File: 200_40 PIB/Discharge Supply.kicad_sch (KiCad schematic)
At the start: 57 parts, among them Q1 EPC2302, T1 Arthur, U1 LM5022MM, U2 TLVH431BQDCKT, U3 LTV-817-C

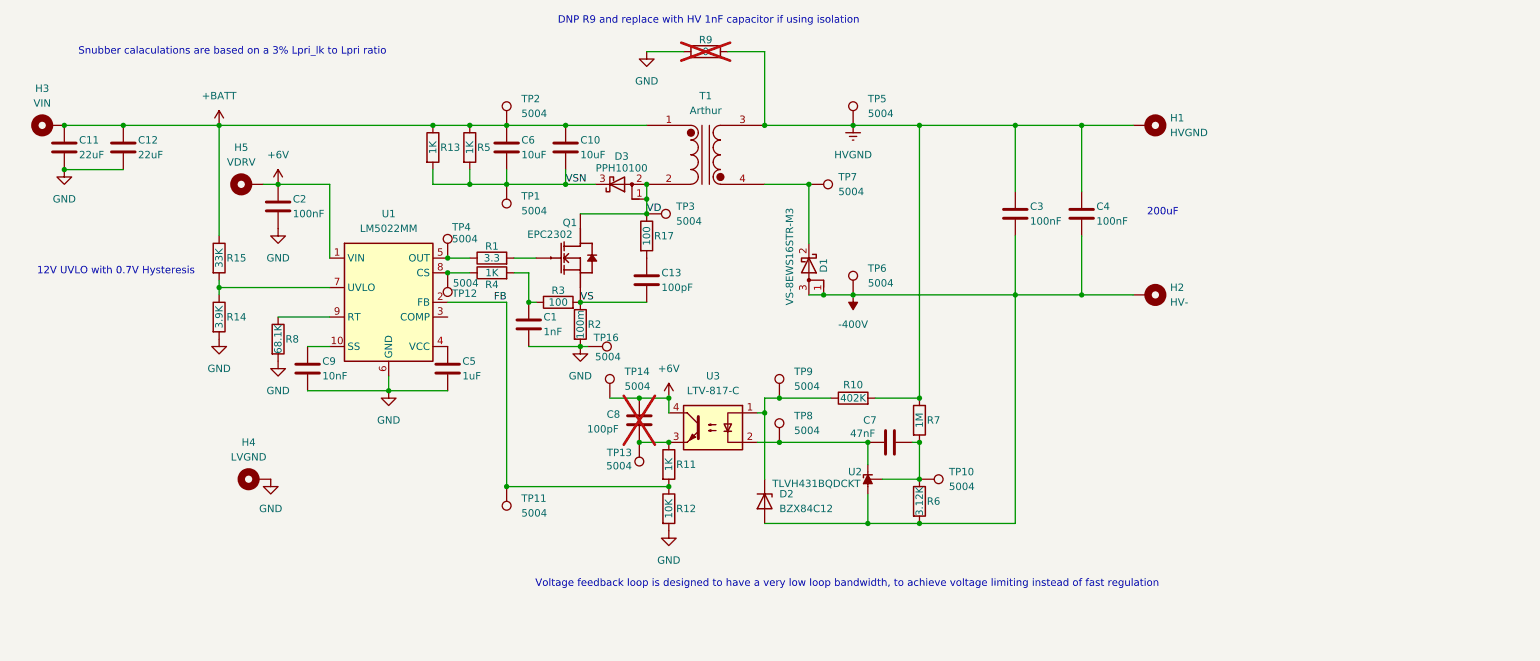
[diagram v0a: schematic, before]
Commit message: Summer 2026 Updates
Created symbol, footprint, and 3D model libraries. Redesigned PIB.
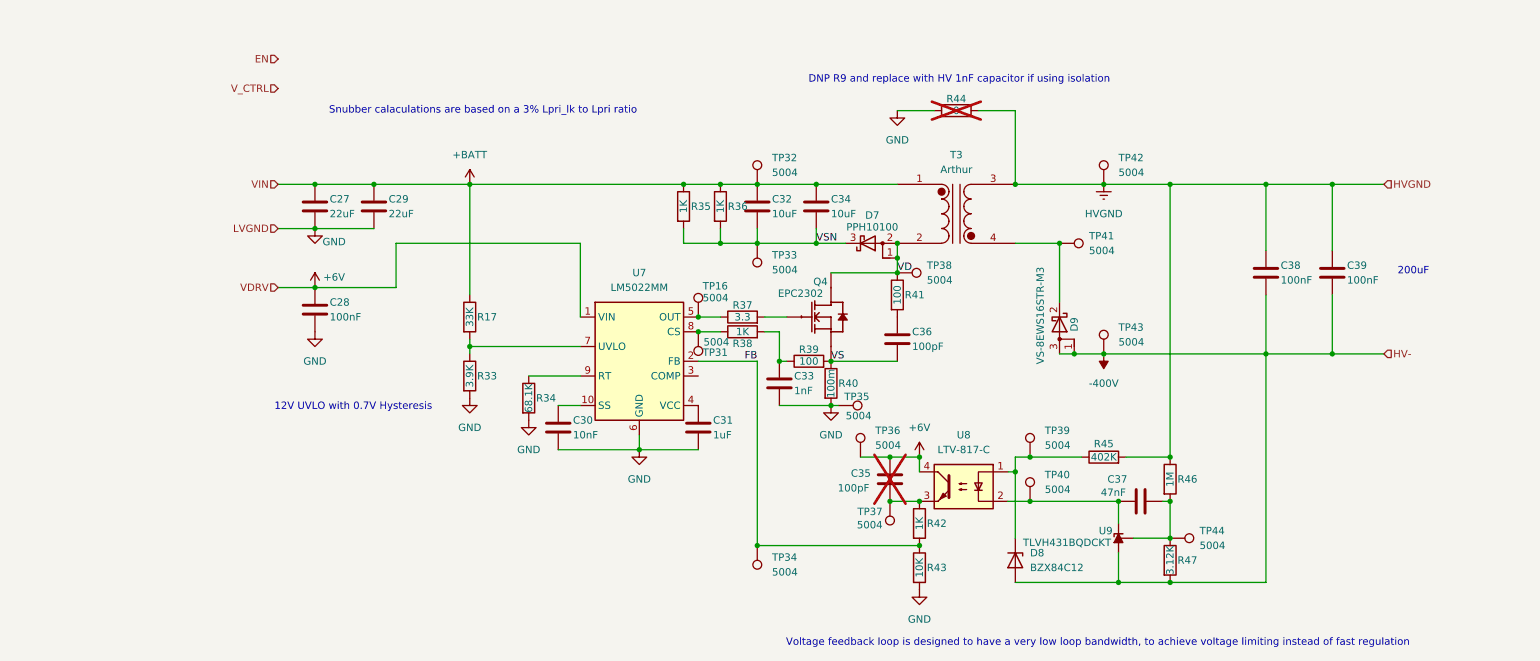
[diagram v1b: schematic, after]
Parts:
- removed C1: 1nF, Capacitor_SMD:C_0402_1005Metric, symbol Device:C
- removed C10, C6: 10uF, Capacitor_SMD:C_1210_3225Metric, symbol Device:C
- removed C11, C12: 22uF, Capacitor_SMD:C_1210_3225Metric, symbol Device:C
- removed C13, C8: 100pF, Capacitor_SMD:C_0603_1608Metric, symbol Device:C
- removed C2: 100nF, Capacitor_SMD:C_0402_1005Metric, symbol Device:C
- removed C3, C4: 100nF, Capacitor_SMD:C_2220_5750Metric, symbol Device:C
- removed C5: 1uF, Capacitor_SMD:C_0402_1005Metric, symbol Device:C
- removed C7: 47nF, Capacitor_SMD:C_0603_1608Metric, symbol Device:C
- removed C9: 10nF, Capacitor_SMD:C_0402_1005Metric, symbol Device:C
- removed D1: VS-8EWS16STR-M3, Package_TO_SOT_SMD:TO-252-2, symbol Device:D_Schottky_AKA
- removed D2: BZX84C12, Package_TO_SOT_SMD:SOT-23, symbol Diode:BZX84Cxx
- removed D3: PPH10100, Package_TO_SOT_SMD:TO-277A, symbol Device:D_Schottky_AAK
- removed H1: HVGND, Pads_Custom:Pad6x4, symbol Mechanical:MountingHole_Pad
- removed H2: HV-, Pads_Custom:Pad6x4, symbol Mechanical:MountingHole_Pad
- removed H3: VIN, Pads_Custom:Pad6x4, symbol Mechanical:MountingHole_Pad
- removed H4: LVGND, Pads_Custom:Pad6x4, symbol Mechanical:MountingHole_Pad
- removed H5: VDRV, Pads_Custom:Pad6x4, symbol Mechanical:MountingHole_Pad
- removed Q1: EPC2302, EPC_FETs:D0606F_100V, symbol EPC_FETs:EPC2302
- removed R1: 3.3, Resistor_SMD:R_0402_1005Metric, symbol Device:R
- removed R10: 402K, Resistor_SMD:R_2512_6332Metric, symbol Device:R
- removed R11: 1K, Resistor_SMD:R_0603_1608Metric, symbol Device:R
- removed R12: 10K, Resistor_SMD:R_0603_1608Metric, symbol Device:R
- removed R13, R5: 1K, Resistor_SMD:R_0805_2012Metric, symbol Device:R
- removed R14: 3.9K, Resistor_SMD:R_0603_1608Metric, symbol Device:R
- removed R15: 33K, Resistor_SMD:R_0603_1608Metric, symbol Device:R
- removed R2: 100m, Resistor_SMD:R_1225_3264Metric, symbol Device:R
- removed R3: 100, Resistor_SMD:R_0402_1005Metric, symbol Device:R
- removed R4: 1K, Resistor_SMD:R_0402_1005Metric, symbol Device:R
- removed R6: 3.12K, Resistor_SMD:R_0603_1608Metric, symbol Device:R
- removed R7: 1M, Resistor_SMD:R_2512_6332Metric, symbol Device:R
- removed R8: 68.1K, Resistor_SMD:R_0402_1005Metric, symbol Device:R
- removed R9: 0, Resistor_SMD:R_2010_5025Metric, symbol Device:R
- removed T1: Arthur, PlanarTransformer:40-2Transformer, symbol transformer:Transformer_1P_1S_Dot
- removed TP1, TP10, TP11, TP12, TP13, TP14, TP2, TP3, TP4, TP5, TP6, TP7, TP8, TP9: 5004, TestPoint:TestPoint_Keystone_5000-5004_Miniature, symbol Connector:TestPoint
- removed U1: LM5022MM, Package_SO:MSOP-10_3x3mm_P0.5mm, symbol Regulator_Switching:LM5022MM
- removed U2: TLVH431BQDCKT, Package_TO_SOT_SMD:SOT-363_SC-70-6, symbol Reference_Voltage:TL431DCK
- removed U3: LTV-817-C, Package_DIP:DIP-4_W7.62mm, symbol Isolator:LTV-817
- added C27, C29: 22uF, Capacitor_SMD:C_1210_3225Metric, symbol Device:C
- added C28: 100nF, Capacitor_SMD:C_0402_1005Metric, symbol Device:C
- added C30: 10nF, Capacitor_SMD:C_0402_1005Metric, symbol Device:C
- added C31: 1uF, Capacitor_SMD:C_0402_1005Metric, symbol Device:C
- added C32, C34: 10uF, Capacitor_SMD:C_1210_3225Metric, symbol Device:C
- added C33: 1nF, Capacitor_SMD:C_0402_1005Metric, symbol Device:C
- added C35, C36: 100pF, Capacitor_SMD:C_0603_1608Metric, symbol Device:C
- added C37: 47nF, Capacitor_SMD:C_0603_1608Metric, symbol Device:C
- added C38, C39: 100nF, Capacitor_SMD:C_2220_5750Metric, symbol Device:C
- added D7: PPH10100, Package_TO_SOT_SMD:TO-277A, symbol Device:D_Schottky_AAK
- added D8: BZX84C12, Package_TO_SOT_SMD:SOT-23, symbol Diode:BZX84Cxx
- added D9: VS-8EWS16STR-M3, Package_TO_SOT_SMD:TO-252-2, symbol Device:D_Schottky_AKA
- added Q4: EPC2302, EPC_FETs:D0606F_100V, symbol EPC_FETs:EPC2302
- added R33: 3.9K, Resistor_SMD:R_0603_1608Metric, symbol Device:R
- added R34: 68.1K, Resistor_SMD:R_0402_1005Metric, symbol Device:R
- added R35, R36: 1K, Resistor_SMD:R_0805_2012Metric, symbol Device:R
- added R37: 3.3, Resistor_SMD:R_0402_1005Metric, symbol Device:R
- added R38: 1K, Resistor_SMD:R_0402_1005Metric, symbol Device:R
- added R39: 100, Resistor_SMD:R_0402_1005Metric, symbol Device:R
- added R40: 100m, Resistor_SMD:R_1225_3264Metric, symbol Device:R
- added R41: 100, Resistor_SMD:R_0603_1608Metric, symbol Device:R
- added R42: 1K, Resistor_SMD:R_0603_1608Metric, symbol Device:R
- added R43: 10K, Resistor_SMD:R_0603_1608Metric, symbol Device:R
- added R44: 0, Resistor_SMD:R_2010_5025Metric, symbol Device:R
- added R45: 402K, Resistor_SMD:R_2512_6332Metric, symbol Device:R
- added R46: 1M, Resistor_SMD:R_2512_6332Metric, symbol Device:R
- added R47: 3.12K, Resistor_SMD:R_0603_1608Metric, symbol Device:R
- added T3: Arthur, PlanarTransformer:40-2Transformer, symbol transformer:Transformer_1P_1S_Dot
- added TP31, TP32, TP33, TP34, TP35, TP36, TP37, TP38, TP39, TP40, TP41, TP42, TP43, TP44: 5004, TestPoint:TestPoint_Keystone_5000-5004_Miniature, symbol Connector:TestPoint
- added U7: LM5022MM, Package_SO:MSOP-10_3x3mm_P0.5mm, symbol Regulator_Switching:LM5022MM
- added U8: LTV-817-C, Package_DIP:DIP-4_W7.62mm, symbol Isolator:LTV-817
- added U9: TLVH431BQDCKT, Package_TO_SOT_SMD:SOT-363_SC-70-6, symbol Reference_Voltage:TL431DCK
- R17: value 100 -> 33K
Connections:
- net +6V: now also C28.1, C35.2, TP36.1, U7.1 (VIN), U8.4
- net +BATT: now also R17.1, C27.1, C29.1, C32.1, C34.1, R35.1, R36.1, T3.1 (AA), TP32.1
- net -400V: now also C38.2, C39.2, D8.1 (A), D9.1 (A), D9.3 (A), R47.2, TP43.1, U9.6 (A)
- net FB: now also R42.2, R43.1, TP34.1, U7.2 (FB)
- net GND: now also C27.2, C28.2, C29.2, C30.2, C31.2, C33.2, R33.2, R34.2, R40.2, R43.2, R44.1, TP35.1, U7.6 (GND); no longer TP16.1
- net HVGND: now also C38.1, C39.1, R44.2, R45.2, R46.1, T3.3 (SA), TP42.1
- net VD: now also D7.1 (A), D7.2 (A), Q4.3 (D), Q4.5 (D), Q4.7 (D), R41.1, T3.2 (AB), TP38.1; no longer R17.1
- net VS: now also C36.2, Q4.2 (S), Q4.4 (S), Q4.6 (S), R39.2, R40.1
- net VSN: now also C32.2, C34.2, D7.3 (K), R35.2, R36.2, TP33.1
- net at R17.2: now also R33.1, U7.7 (UVLO)
- new net: C36.1, R41.2
- new net: D8.3 (K), R45.1, TP39.1, U8.1
- new net: C37.1, TP40.1, U8.2, U9.1 (K)
- new net: C37.2, R46.2, R47.1, TP44.1, U9.3 (REF)
- new net: C33.1, R38.2, R39.1
- new net: D9.2 (K), T3.4 (SB), TP41.1
- new net: R38.1, TP31.1, U7.8 (CS)
- new net: C30.1, U7.10 (SS)
- new net: C31.1, U7.4 (VCC)
- new net: R37.1, TP16.1, U7.5 (OUT)
- new net: R34.1, U7.9 (RT)
- new net: C35.1, R42.1, TP37.1, U8.3
- new net: Q4.1 (G), R37.2

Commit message: pretty pib that doesnt work
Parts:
- removed TP16, TP31, TP32, TP33, TP35, TP37, TP38, TP39, TP40: 5004, TestPoint:TestPoint_Keystone_5000-5004_Miniature, symbol Connector:TestPoint
